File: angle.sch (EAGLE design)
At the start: 12 parts

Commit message: fixed up right angle
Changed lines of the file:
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@@
 <?xml version="1.0" encoding="utf-8"?>
 <!DOCTYPE eagle SYSTEM "eagle.dtd">
-<eagle version="8.7.0">
+<eagle version="9.3.0">
 <drawing>
 <settings>
-<setting alwaysvectorfont="yes"/>
+<setting alwaysvectorfont="no"/>
 <setting keepoldvectorfont="yes"/>
 <setting verticaltext="up"/>
@@
 </plain>
 <instances>
-<instance part="VCC-CLIP" gate="CLIP" x="-33.02" y="-2.54"/>
-<instance part="GND-CLIP" gate="CLIP" x="-68.58" y="15.24"/>
-<instance part="GND10" gate="1" x="-58.42" y="12.7"/>
-<instance part="GND11" gate="1" x="-58.42" y="5.08"/>
-<instance part="PWM-CLIP" gate="CLIP" x="-60.96" y="-25.4"/>
-<instance part="VCC-CLIP3" gate="CLIP" x="-33.02" y="7.62"/>
-<instance part="GND-CLIP3" gate="CLIP" x="-68.58" y="-10.16"/>
-<instance part="GND6" gate="1" x="-58.42" y="-12.7"/>
-<instance part="PWM-CLIP1" gate="CLIP" x="-30.48" y="-25.4"/>
-<instance part="FRAME1" gate="G$1" x="-114.3" y="-81.28"/>
-<instance part="VCC-CLIP1" gate="CLIP" x="58.42" y="5.08"/>
-<instance part="GND-CLIP1" gate="CLIP" x="22.86" y="22.86"/>
-<instance part="GND1" gate="1" x="33.02" y="20.32"/>
-<instance part="GND2" gate="1" x="33.02" y="12.7"/>
-<instance part="PWM-CLIP2" gate="CLIP" x="30.48" y="-17.78"/>
-<instance part="VCC-CLIP2" gate="CLIP" x="58.42" y="15.24"/>
-<instance part="GND-CLIP2" gate="CLIP" x="22.86" y="-2.54"/>
-<instance part="GND3" gate="1" x="33.02" y="-5.08"/>
-<instance part="PWM-CLIP3" gate="CLIP" x="60.96" y="-17.78"/>
+<instance part="VCC-CLIP" gate="CLIP" x="-33.02" y="-2.54" smashed="yes"/>
+<instance part="GND-CLIP" gate="CLIP" x="-68.58" y="15.24" smashed="yes"/>
+<instance part="GND10" gate="1" x="-58.42" y="12.7" smashed="yes">
+<attribute name="VALUE" x="-60.96" y="10.16" size="1.778" layer="96"/>
+</instance>
+<instance part="GND11" gate="1" x="-58.42" y="5.08" smashed="yes">
+<attribute name="VALUE" x="-60.96" y="2.54" size="1.778" layer="96"/>
+</instance>
+<instance part="PWM-CLIP" gate="CLIP" x="-60.96" y="-25.4" smashed="yes"/>
+<instance part="VCC-CLIP3" gate="CLIP" x="-33.02" y="7.62" smashed="yes"/>
+<instance part="GND-CLIP3" gate="CLIP" x="-68.58" y="-10.16" smashed="yes"/>
+<instance part="GND6" gate="1" x="-58.42" y="-12.7" smashed="yes">
+<attribute name="VALUE" x="-60.96" y="-15.24" size="1.778" layer="96"/>
+</instance>
+<instance part="PWM-CLIP1" gate="CLIP" x="-30.48" y="-25.4" smashed="yes"/>
+<instance part="FRAME1" gate="G$1" x="-114.3" y="-81.28" smashed="yes">
+<attribute name="DRAWING_NAME" x="102.87" y="-66.04" size="2.54" layer="94"/>
+<attribute name="LAST_DATE_TIME" x="102.87" y="-71.12" size="2.286" layer="94"/>
+<attribute name="SHEET" x="116.205" y="-76.2" size="2.54" layer="94"/>
+</instance>
+<instance part="VCC-CLIP1" gate="CLIP" x="58.42" y="5.08" smashed="yes"/>
+<instance part="GND-CLIP1" gate="CLIP" x="22.86" y="22.86" smashed="yes"/>
+<instance part="GND1" gate="1" x="33.02" y="20.32" smashed="yes">
+<attribute name="VALUE" x="30.48" y="17.78" size="1.778" layer="96"/>
+</instance>
+<instance part="GND2" gate="1" x="33.02" y="12.7" smashed="yes">
+<attribute name="VALUE" x="30.48" y="10.16" size="1.778" layer="96"/>
+</instance>
+<instance part="PWM-CLIP2" gate="CLIP" x="30.48" y="-17.78" smashed="yes"/>
+<instance part="VCC-CLIP2" gate="CLIP" x="58.42" y="15.24" smashed="yes"/>
+<instance part="GND-CLIP2" gate="CLIP" x="22.86" y="-2.54" smashed="yes"/>
+<instance part="GND3" gate="1" x="33.02" y="-5.08" smashed="yes">
+<attribute name="VALUE" x="30.48" y="-7.62" size="1.778" layer="96"/>
+</instance>
+<instance part="PWM-CLIP3" gate="CLIP" x="60.96" y="-17.78" smashed="yes"/>
 </instances>
 <busses>

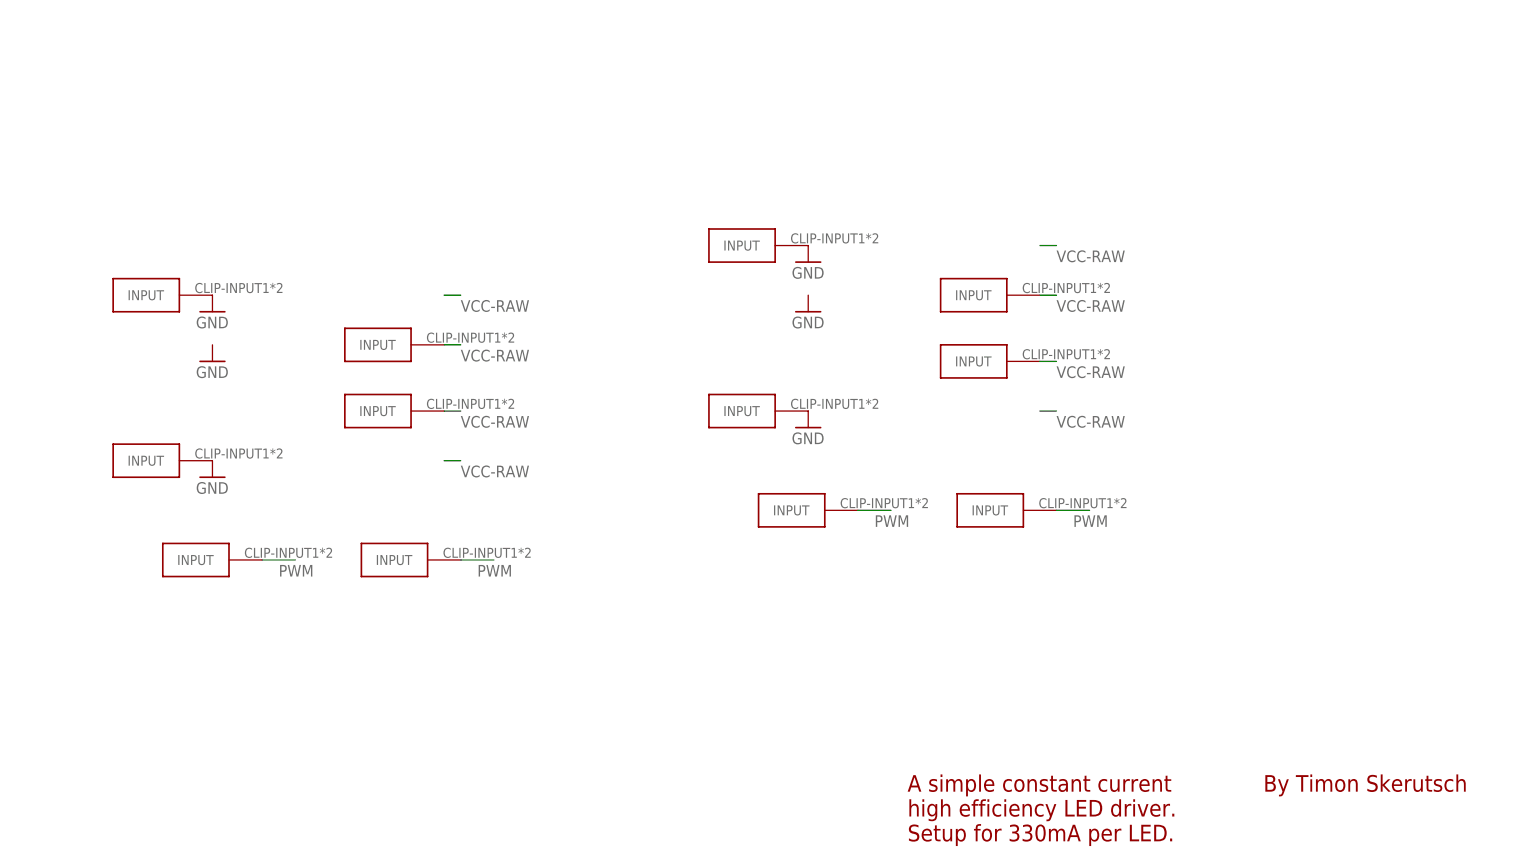
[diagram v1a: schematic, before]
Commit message: doubled and mirrored angle pcb
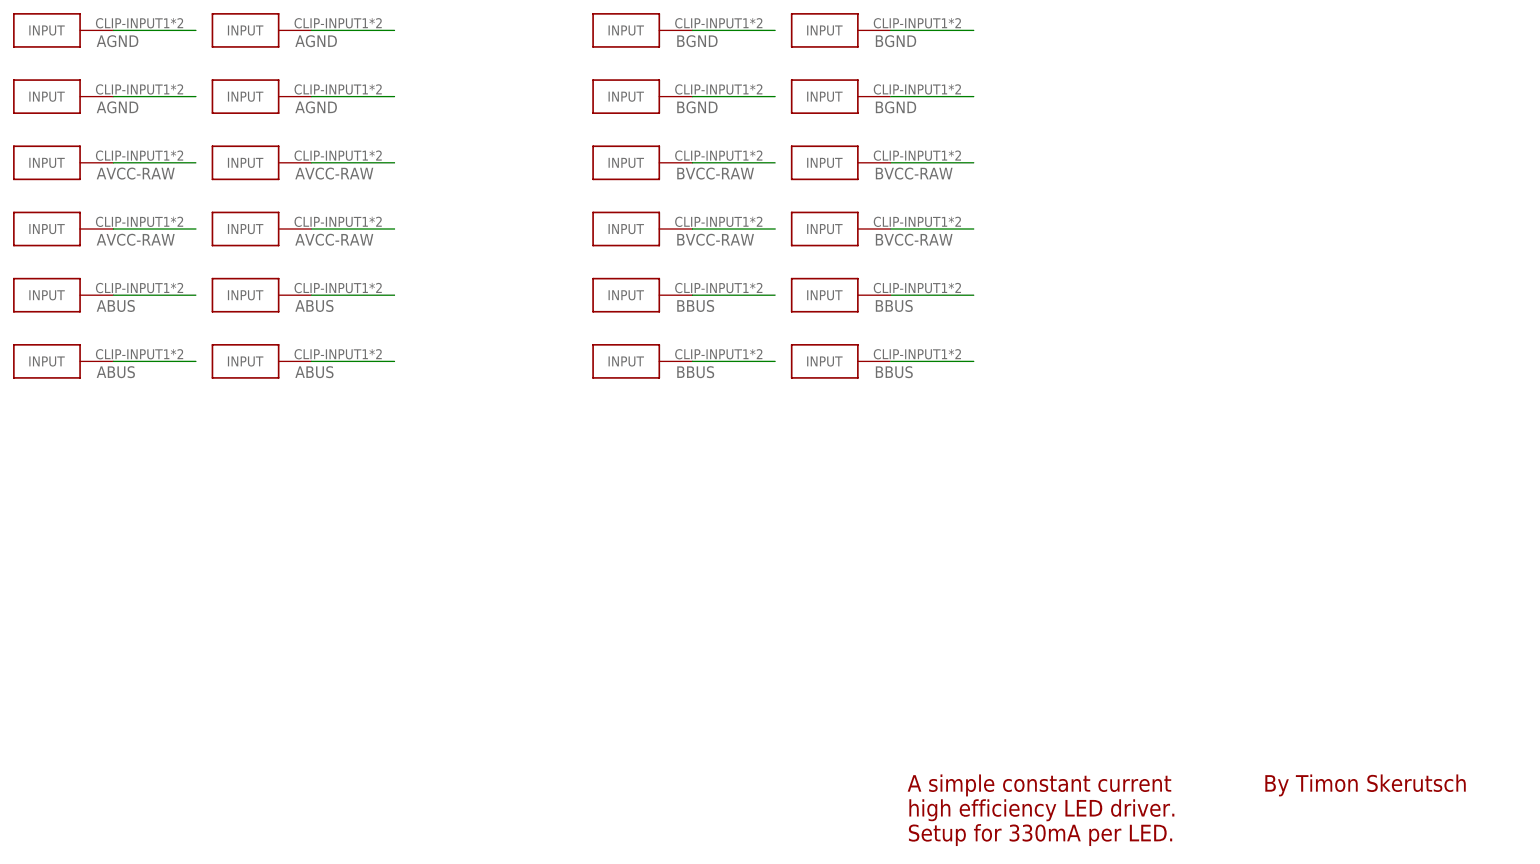
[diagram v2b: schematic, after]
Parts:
- removed GND-CLIP, GND-CLIP1, GND-CLIP2, GND-CLIP3, PWM-CLIP, PWM-CLIP1, PWM-CLIP2, PWM-CLIP3, VCC-CLIP, VCC-CLIP1, VCC-CLIP2, VCC-CLIP3: FUSE-HOLDER-5X20MM, timon-diverses:FUSE-HOLDER-5X20MM
- added ABUS-CLIP, ABUS-CLIP1, ABUS-CLIP2, ABUS-CLIP3, AGND-CLIP, AGND-CLIP1, AGND-CLIP2, AGND-CLIP3, AVCC-CLIP, AVCC-CLIP1, AVCC-CLIP2, AVCC-CLIP3, BBUS-CLIP, BBUS-CLIP1, BBUS-CLIP2, BBUS-CLIP3, BGND-CLIP, BGND-CLIP1, BGND-CLIP2, BGND-CLIP3, BVCC-CLIP, BVCC-CLIP1, BVCC-CLIP2, BVCC-CLIP3: FUSE-HOLDER-5X20MM, timon-diverses:FUSE-HOLDER-5X20MM
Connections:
- removed net GND: GND-CLIP.INPUT, GND-CLIP1.INPUT, GND-CLIP2.INPUT, GND-CLIP3.INPUT
- removed net PWM: PWM-CLIP.INPUT, PWM-CLIP1.INPUT, PWM-CLIP2.INPUT, PWM-CLIP3.INPUT
- removed net VCC-RAW: VCC-CLIP.INPUT, VCC-CLIP1.INPUT, VCC-CLIP2.INPUT, VCC-CLIP3.INPUT
- new net ABUS: ABUS-CLIP.INPUT, ABUS-CLIP1.INPUT, ABUS-CLIP2.INPUT, ABUS-CLIP3.INPUT
- new net AGND: AGND-CLIP.INPUT, AGND-CLIP1.INPUT, AGND-CLIP2.INPUT, AGND-CLIP3.INPUT
- new net AVCC-RAW: AVCC-CLIP.INPUT, AVCC-CLIP1.INPUT, AVCC-CLIP2.INPUT, AVCC-CLIP3.INPUT
- new net BBUS: BBUS-CLIP.INPUT, BBUS-CLIP1.INPUT, BBUS-CLIP2.INPUT, BBUS-CLIP3.INPUT
- new net BGND: BGND-CLIP.INPUT, BGND-CLIP1.INPUT, BGND-CLIP2.INPUT, BGND-CLIP3.INPUT
- new net BVCC-RAW: BVCC-CLIP.INPUT, BVCC-CLIP1.INPUT, BVCC-CLIP2.INPUT, BVCC-CLIP3.INPUT
